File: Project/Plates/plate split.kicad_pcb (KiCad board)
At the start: 2 copper layers, 242.9 x 88.2 mm, 46 parts

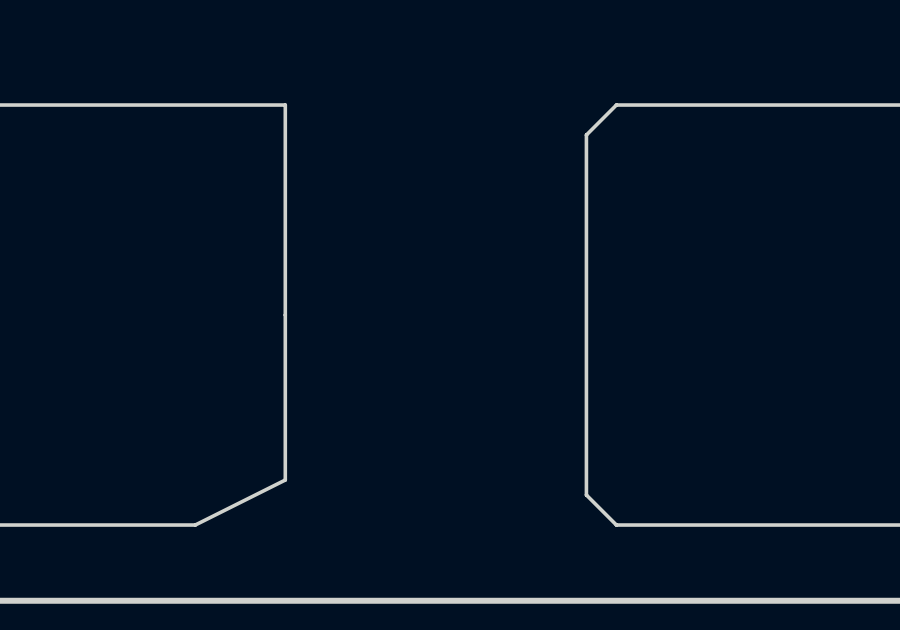
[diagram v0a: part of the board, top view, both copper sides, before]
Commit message: pcb & plate revision
move mux, add cutout for all plates for boot
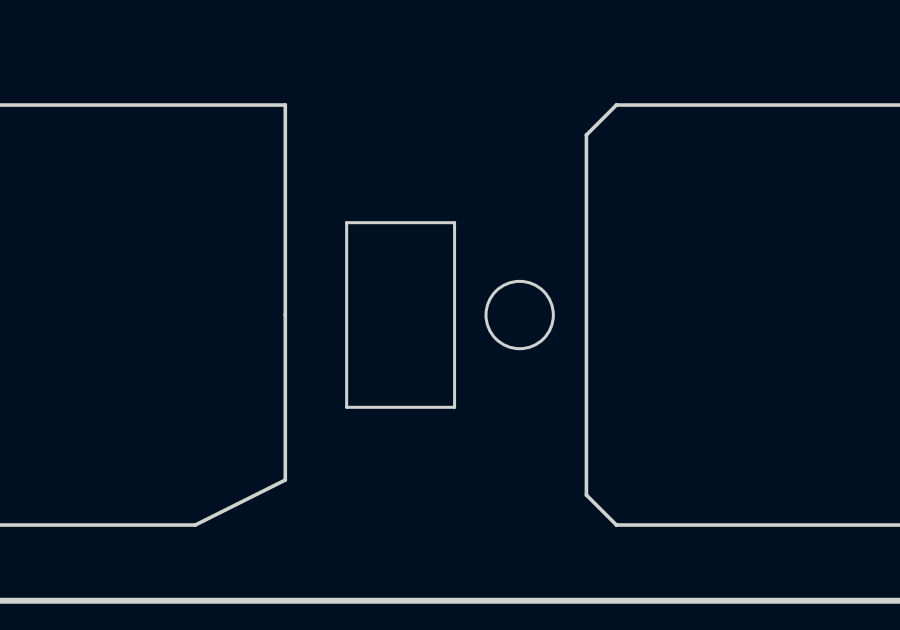
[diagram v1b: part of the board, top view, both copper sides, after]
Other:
- outline, holes or cut-outs redrawn
